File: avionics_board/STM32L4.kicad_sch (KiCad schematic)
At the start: 30 parts, among them U1 STM32L496ZGTx

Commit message: add headers for ACS and sun sensors
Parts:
- added R41: 100K, Resistor_SMD:R_0402_1005Metric_Pad0.72x0.64mm_HandSolder, symbol Device:R
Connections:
- net 3.3V_STM_CORE: now also R41.1
- net SOLAR_INT_EXTI11: now also R41.2
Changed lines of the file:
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@@
 	(wire
 		(pts
+			(xy 259.08 186.69) (xy 241.3 186.69)
+		)
+		(stroke
+			(width 0)
+			(type default)
+		)
+	)
+	(wire
+		(pts
 			(xy 62.865 224.79) (xy 57.15 224.79)
 		)
@@
 	(hierarchical_label "SOLAR_INT_EXTI11"
 		(shape input)
-		(at 241.3 186.69 0)
+		(at 259.08 186.69 0)
 		(fields_autoplaced yes)
 		(effects
@@
 		)
 	)
+	(hierarchical_label "3.3V_STM_CORE"
+		(shape input)
+		(at 259.08 179.07 0)
+		(fields_autoplaced yes)
+		(effects
+			(font
+				(size 1.27 1.27)
+			)
+			(justify left)
+		)
+	)
 	(hierarchical_label "GPS_PPS_EXTI9"
 		(shape input)
@@
 					(unit 1)
 				)
+			)
+		)
+	)
+	(symbol
+		(lib_id "Device:R")
+		(at 259.08 182.88 0)
+		(unit 1)
+		(exclude_from_sim no)
+		(in_bom yes)
+		(on_board yes)
+		(dnp no)
+		(fields_autoplaced yes)
+		(property "Reference" "R41"
+			(at 261.62 181.6099 0)
+			(effects
+				(font
+					(size 1.27 1.27)
+				)
+				(justify left)
+			)
+		)
+		(property "Value" "100K"
+			(at 261.62 184.1499 0)
+			(effects
+				(font
+					(size 1.27 1.27)
+				)
+				(justify left)
+			)
+		)
+		(property "Footprint" "Resistor_SMD:R_0402_1005Metric_Pad0.72x0.64mm_HandSolder"
+			(at 257.302 182.88 90)
+			(effects
+				(font
+					(size 1.27 1.27)
+				)
+				(hide yes)
+			)
+		)
+		(property "Datasheet" "https://www.yageo.com/upload/media/product/products/datasheet/rchip/PYu-RC_Group_51_RoHS_L_12.pdf"
+			(at 259.08 182.88 0)
+			(effects
+				(font
+					(size 1.27 1.27)
+				)
+				(hide yes)
+			)
+		)
+		(property "Description" "Resistor"
+			(at 259.08 182.88 0)
+			(effects
+				(font
+					(size 1.27 1.27)
+				)
+				(hide yes)
+			)
+		)
+		(property "Manufacturer" "YAGEO"
+			(at 259.08 182.88 0)
+			(effects
+				(font
+					(size 1.27 1.27)
+				)
+				(hide yes)
+			)
+		)
+		(property "Part Number" "RC0402FR-07100KL"
+			(at 259.08 182.88 0)
+			(effects
+				(font
+					(size 1.27 1.27)
+				)
+				(hide yes)
+			)
+		)
+		(property "Tolerance" "1"
+			(at 259.08 182.88 0)
+			(effects
+				(font
+					(size 1.27 1.27)
+				)
+				(hide yes)
+			)
+		)
+		(pin "1"
+		)
+		(pin "2"
+		)
+		(instances
+			(project "AVIONICS_BOARD"
+				(path "/f6cc00ab-17f1-4973-862f-7ac95fe70668/00000000-0000-0000-0000-00005ea31c93"
+					(reference "R41")
+					(unit 1)
+				)

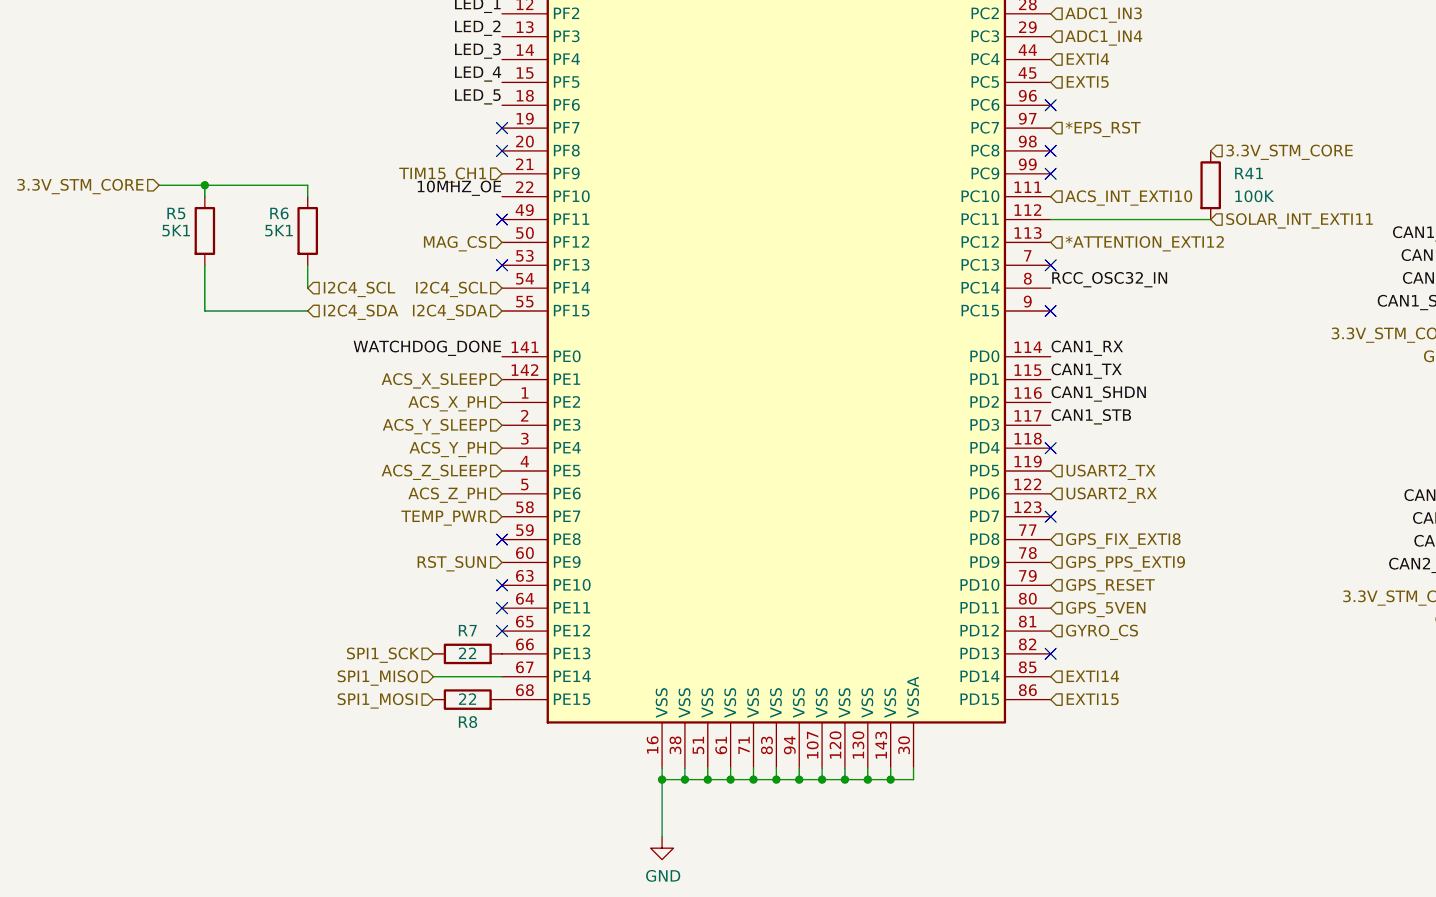
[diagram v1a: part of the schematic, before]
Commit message: use SAMTEC connectors for AVI to side panels, try HARWIN ones next
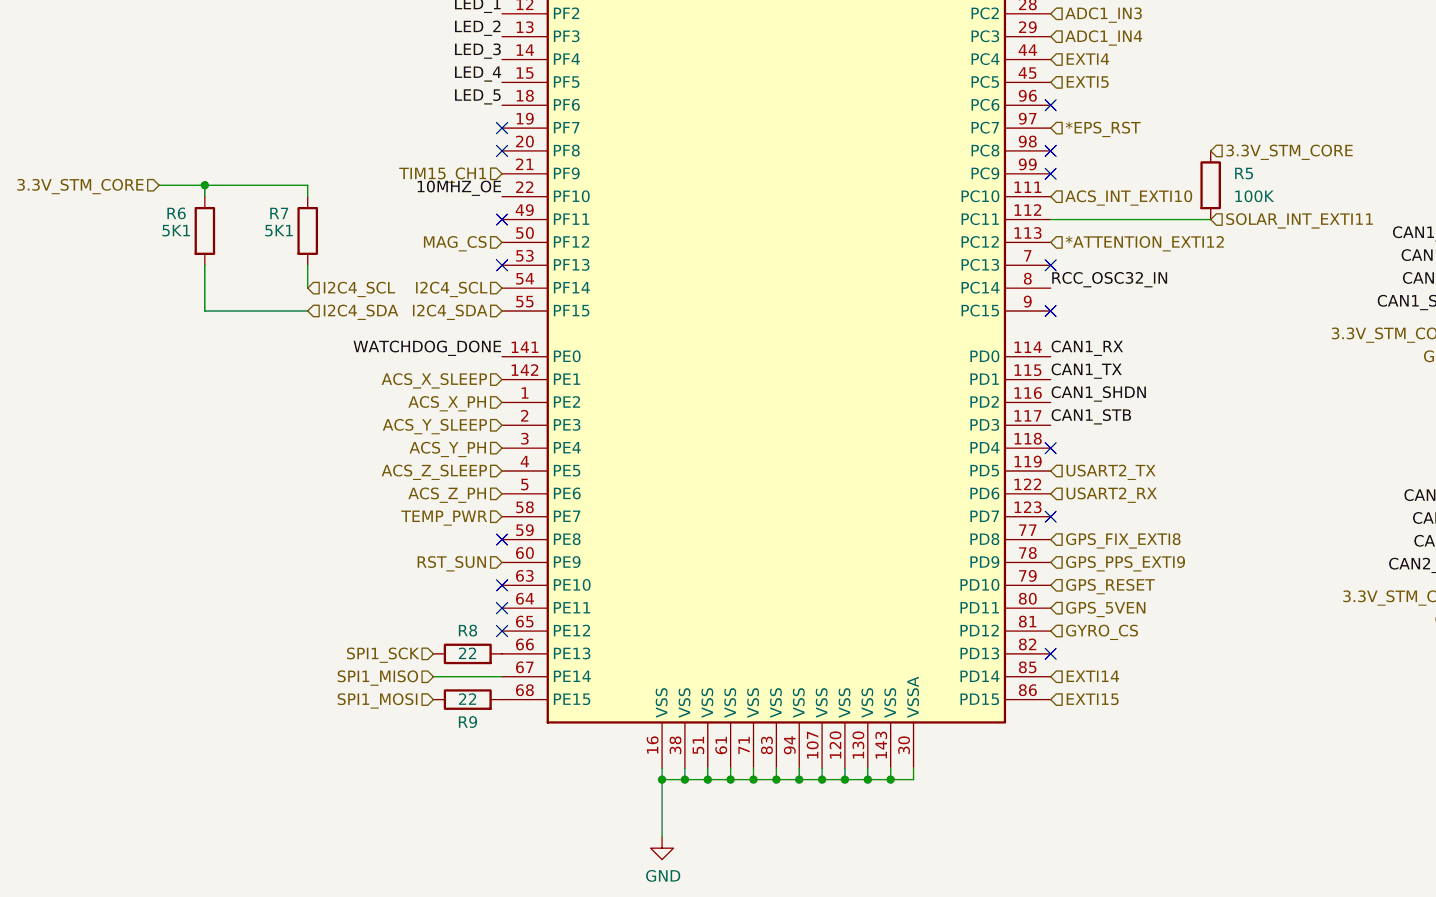
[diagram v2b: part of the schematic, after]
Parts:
- renumbered R41 to R5, R5 to R6, R6 to R7, R7 to R8, R8 to R9
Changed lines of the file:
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@@
 		(on_board yes)
 		(dnp no)
-		(property "Reference" "R6"
+		(property "Reference" "R7"
 			(at 155.575 186.055 0)
 			(effects
@@
 			(project ""
 				(path "/f6cc00ab-17f1-4973-862f-7ac95fe70668/00000000-0000-0000-0000-00005ea31c93"
-					(reference "R6")
+					(reference "R7")
 					(unit 1)
 				)
@@
 		(on_board yes)
 		(dnp no)
-		(property "Reference" "R5"
+		(property "Reference" "R6"
 			(at 144.145 186.055 0)
 			(effects
@@
 			(project ""
 				(path "/f6cc00ab-17f1-4973-862f-7ac95fe70668/00000000-0000-0000-0000-00005ea31c93"
-					(reference "R5")
+					(reference "R6")
 					(unit 1)
 				)
@@
 		(on_board yes)
 		(dnp no)
-		(property "Reference" "R7"
+		(property "Reference" "R8"
 			(at 176.53 232.41 90)
 			(effects
@@
 			(project "AVIONICS_BOARD"
 				(path "/f6cc00ab-17f1-4973-862f-7ac95fe70668/00000000-0000-0000-0000-00005ea31c93"
-					(reference "R7")
+					(reference "R8")
 					(unit 1)
 				)
@@
 		(dnp no)
 		(fields_autoplaced yes)
-		(property "Reference" "R41"
+		(property "Reference" "R5"
 			(at 261.62 181.6099 0)
 			(effects
@@
 			(project "AVIONICS_BOARD"
 				(path "/f6cc00ab-17f1-4973-862f-7ac95fe70668/00000000-0000-0000-0000-00005ea31c93"
-					(reference "R41")
+					(reference "R5")
 					(unit 1)
 				)
@@
 		(on_board yes)
 		(dnp no)
-		(property "Reference" "R8"
+		(property "Reference" "R9"
 			(at 176.53 242.57 90)
 			(effects
@@
 			(project "AVIONICS_BOARD"
 				(path "/f6cc00ab-17f1-4973-862f-7ac95fe70668/00000000-0000-0000-0000-00005ea31c93"
-					(reference "R8")
+					(reference "R9")
 					(unit 1)
 				)

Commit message: AVI: using through hole M50 connectors for sun detectors and ACS
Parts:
- C1, C11, C12, C13, C14, C15, C17, C18, C2, C3, C4, C6, C8, C9: Order https://www.digikey.com/product-detail/en/samsung-electro-m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 -> (none)
- C10, C5, C7: Order https://www.digikey.com/product-detail/en/tdk-corporation/C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 -> (none)
- C16, C19, C20: Order https://www.digikey.com/en/products/detail/samsung-electro-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 -> (none)
- U1: Order https://www.digikey.com/product-detail/en/stmicroelectronic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 -> (none)
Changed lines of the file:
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@@
 			)
 		)
-		(property "Order" "https://www.digikey.com/product-detail/en/samsung-electro-mechanics/CL10B104KA8NNNC/1276-1006-1-ND/3889092"
-			(at 186.69 21.59 90)
-			(effects
-				(font
-					(size 1.27 1.27)
-				)
-				(hide yes)
-			)
-		)
 		(property "Voltage" "25"
 			(at 182.88 20.32 90)
@@
 			)
 		)
-		(property "Order" ""
-			(at 158.75 187.96 0)
-			(effects
-				(font
-					(size 1.27 1.27)
-				)
-				(hide yes)
-			)
-		)
 		(property "Alt" ""
 			(at 158.75 187.96 0)
@@
 			)
 		)
-		(property "Order" ""
-			(at 147.32 187.96 0)
-			(effects
-				(font
-					(size 1.27 1.27)
-				)
-				(hide yes)
-			)
-		)
 		(property "Alt" ""
 			(at 147.32 187.96 0)
@@
 			)
 		)
-		(property "Order" ""
-			(at 158.115 142.24 0)
-			(effects
-				(font
-					(size 1.27 1.27)
-				)
-				(hide yes)
-			)
-		)
 		(property "Alt" ""
 			(at 158.115 142.24 0)
@@
 			)
 		)
-		(property "Order" ""
-			(at 147.955 142.24 0)
-			(effects
-				(font
-					(size 1.27 1.27)
-				)
-				(hide yes)
-			)
-		)
 		(property "Alt" ""
 			(at 147.955 142.24 0)
@@
 			)
 		)
-		(property "Order" "https://www.digikey.com/product-detail/en/stmicroelectronics/STM32L496ZGT3/497-17177-ND/6709882"
-			(at 210.82 156.21 0)
-			(effects
-				(font
-					(size 1.27 1.27)
-				)
-				(hide yes)
-			)
-		)
 		(property "Alt" ""
 			(at 210.82 156.21 0)
@@
 			)
 		)
-		(property "Order" "https://www.digikey.com/product-detail/en/samsung-electro-mechanics/CL10B105KP8NFNC/1276-1945-1-ND/3890031"
-			(at 215.9 31.75 90)
-			(effects
-				(font
-					(size 1.27 1.27)
-				)
-				(hide yes)
-			)
-		)
 		(property "Voltage" "16"
 			(at 212.725 30.48 90)
@@
 			)
 		)
-		(property "Order" "https://www.digikey.com/en/products/detail/samsung-electro-mechanics/CL10B103KB8NNNC/3886667"
-			(at 163.83 81.28 90)
-			(effects
-				(font
-					(size 1.27 1.27)
-				)
-				(hide yes)
-			)
-		)
 		(property "Voltage" "25"
 			(at 167.64 81.28 0)
@@
 			)
 		)
-		(property "Order" "https://www.digikey.com/en/products/detail/samsung-electro-mechanics/CL10B103KB8NNNC/3886667"
-			(at 172.72 81.28 90)
-			(effects
-				(font
-					(size 1.27 1.27)
-				)
-				(hide yes)
-			)
-		)
 		(property "Voltage" "16"
 			(at 176.53 81.28 0)
@@
 			)
 		)
-		(property "Order" "https://www.digikey.com/product-detail/en/samsung-electro-mechanics/CL10B104KA8NNNC/1276-1006-1-ND/3889092"
-			(at 186.69 33.02 90)
-			(effects
-				(font
-					(size 1.27 1.27)
-				)
-				(hide yes)
-			)
-		)
 		(property "Voltage" "25"
 			(at 182.88 31.75 90)
@@
 			)
 		)
-		(property "Order" "https://www.digikey.com/product-detail/en/samsung-electro-mechanics/CL10B104KA8NNNC/1276-1006-1-ND/3889092"
-			(at 186.69 39.37 90)
-			(effects
-				(font
-					(size 1.27 1.27)
-				)
-				(hide yes)
-			)
-		)
 		(property "Voltage" "25"
 			(at 182.88 38.1 90)
@@
 			)
 		)
-		(property "Order" "https://www.digikey.com/product-detail/en/samsung-electro-mechanics/CL10B104KA8NNNC/1276-1006-1-ND/3889092"
-			(at 186.69 44.45 90)
-			(effects
-				(font
-					(size 1.27 1.27)
-				)
-				(hide yes)
-			)
-		)
 		(property "Voltage" "25"
 			(at 182.88 43.18 90)
@@
 			)
 		)
-		(property "Order" "https://www.digikey.com/product-detail/en/samsung-electro-mechanics/CL10B104KA8NNNC/1276-1006-1-ND/3889092"
-			(at 186.69 50.8 90)
-			(effects
-				(font
-					(size 1.27 1.27)
-				)
-				(hide yes)
-			)
-		)
 		(property "Voltage" "25"
 			(at 182.88 49.53 90)
@@
 			)
 		)
-		(property "Order" "https://www.digikey.com/product-detail/en/samsung-electro-mechanics/CL10B104KA8NNNC/1276-1006-1-ND/3889092"
-			(at 186.69 55.88 90)
-			(effects
-				(font
-					(size 1.27 1.27)
-				)
-				(hide yes)
-			)
-		)
 		(property "Voltage" "25"
 			(at 182.88 54.61 90)
@@
 			)
 		)
-		(property "Order" "https://www.digikey.com/product-detail/en/samsung-electro-mechanics/CL10B104KA8NNNC/1276-1006-1-ND/3889092"
-			(at 198.12 50.8 90)
-			(effects
-				(font
-					(size 1.27 1.27)
-				)
-				(hide yes)
-			)
-		)
 		(property "Voltage" "25"
 			(at 194.31 49.53 90)
@@
 			)
 		)
-		(property "Order" "https://www.digikey.com/product-detail/en/samsung-electro-mechanics/CL10B104KA8NNNC/1276-1006-1-ND/3889092"
-			(at 198.12 55.88 90)
-			(effects
-				(font
-					(size 1.27 1.27)
-				)
-				(hide yes)
-			)
-		)
 		(property "Voltage" "25"
 			(at 194.31 54.61 90)
@@
 			)
 		)
-		(property "Order" "https://www.digikey.com/product-detail/en/samsung-electro-mechanics/CL10B104KA8NNNC/1276-1006-1-ND/3889092"
-			(at 232.41 41.91 90)
-			(effects
-				(font
-					(size 1.27 1.27)
-				)
-				(hide yes)
-			)
-		)
 		(property "Voltage" "25"
 			(at 231.14 38.1 90)
@@
 			)
 		)
-		(property "Order" "https://www.digikey.com/product-detail/en/tdk-corporation/C1608X7S1A475K080AC/445-14258-1-ND/3955924"
-			(at 198.12 39.37 90)
-			(effects
-				(font
-					(size 1.27 1.27)
-				)
-				(hide yes)
-			)
-		)
 		(property "Voltage" "25"
 			(at 194.31 38.1 90)
@@
 			)
 		)
-		(property "Order" "https://www.digikey.com/en/products/detail/samsung-electro-mechanics/CL10B103KB8NNNC/3886667"
-			(at 215.9 50.8 90)
-			(effects
-				(font
-					(size 1.27 1.27)
-				)
-				(hide yes)
-			)
-		)
 		(property "Voltage" "25"
 			(at 211.455 49.53 90)
@@
 			)
 		)
-		(property "Order" "https://www.digikey.com/product-detail/en/samsung-electro-mechanics/CL10B104KA8NNNC/1276-1006-1-ND/3889092"
-			(at 186.69 27.94 90)
-			(effects
-				(font
-					(size 1.27 1.27)
-				)
-				(hide yes)
-			)
-		)
 		(property "Voltage" "25"
 			(at 182.88 26.67 90)
@@
 			)
 		)
-		(property "Order" "https://www.digikey.com/product-detail/en/samsung-electro-mechanics/CL10B104KA8NNNC/1276-1006-1-ND/3889092"
-			(at 237.49 41.91 90)
-			(effects
-				(font
-					(size 1.27 1.27)
-				)
-				(hide yes)
-			)
-		)
 		(property "Voltage" "25"
 			(at 236.22 38.1 90)
@@
 			)
 		)
-		(property "Order" "https://www.digikey.com/product-detail/en/tdk-corporation/C1608X7S1A475K080AC/445-14258-1-ND/3955924"
-			(at 242.57 41.91 90)
-			(effects
-				(font
-					(size 1.27 1.27)
-				)
-				(hide yes)
-			)
-		)
 		(property "Voltage" "25"
 			(at 241.3 38.1 90)
@@
 			)
 		)
-		(property "Order" "https://www.digikey.com/product-detail/en/tdk-corporation/C1608X7S1A475K080AC/445-14258-1-ND/3955924"
-			(at 198.12 33.02 90)
-			(effects
-				(font
-					(size 1.27 1.27)
-				)
-				(hide yes)
-			)
-		)
 		(property "Voltage" "25"
 			(at 194.31 31.75 90)
@@
 			)
 		)
-		(property "Order" "https://www.digikey.com/product-detail/en/samsung-electro-mechanics/CL10B104KA8NNNC/1276-1006-1-ND/3889092"
-			(at 198.12 44.45 90)
-			(effects
-				(font
-					(size 1.27 1.27)
-				)
-				(hide yes)
-			)
-		)
 		(property "Voltage" "25"
 			(at 194.31 43.18 90)
@@
 			(effects
 				(font
-					(size 1.27 1.27)
-				)
-				(hide yes)
-			)
-		)
-		(property "Order" "https://www.digikey.com/product-detail/en/samsung-electro-mechanics/CL10B105KP8NFNC/1276-1945-1-ND/3890031"
-			(at 215.9 45.72 90)
-			(effects
-				(font
